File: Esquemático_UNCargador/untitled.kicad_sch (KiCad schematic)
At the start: 17 parts

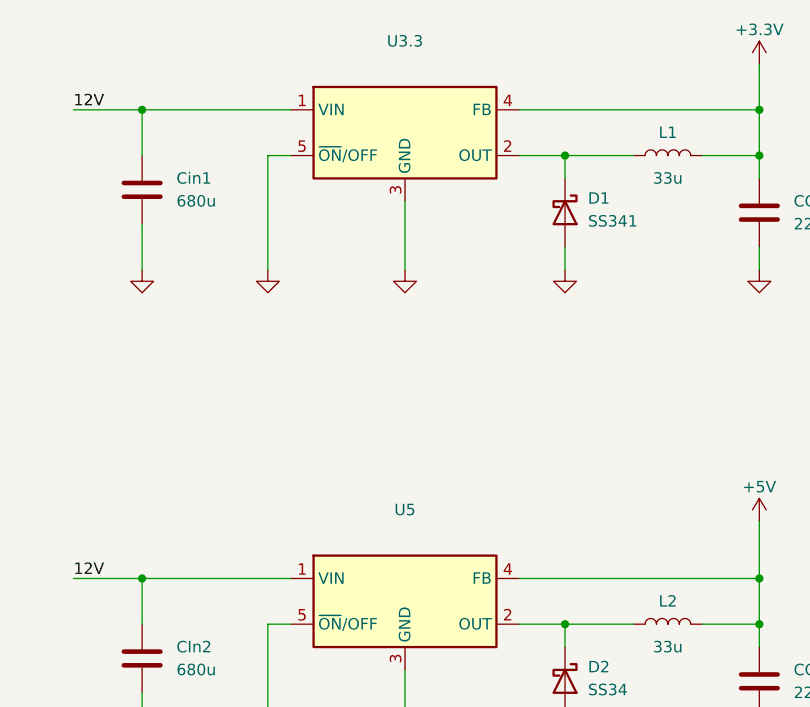
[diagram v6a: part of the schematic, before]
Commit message: LM2596-HuellaActualizada
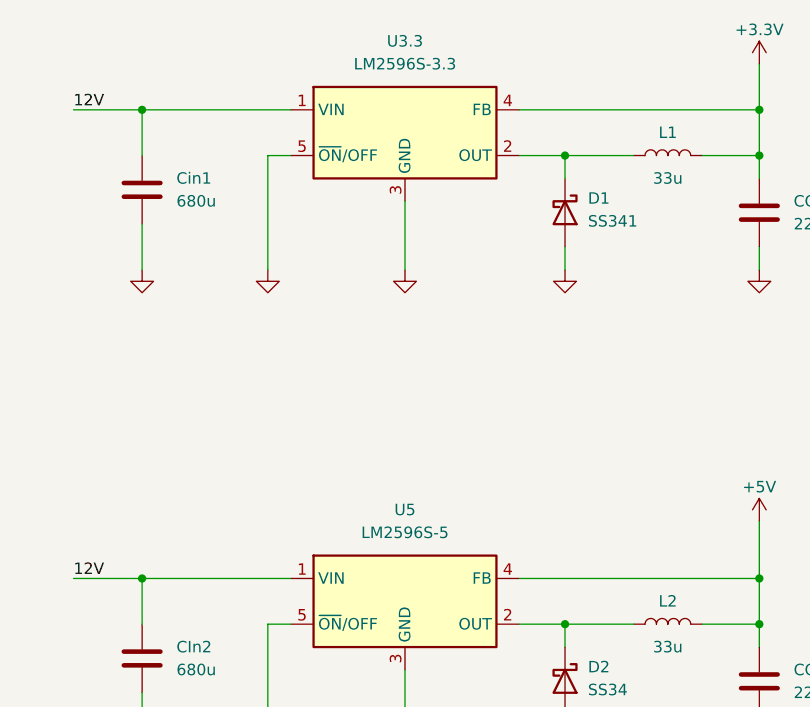
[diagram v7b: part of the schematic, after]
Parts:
- U3.3: value ~ -> LM2596S-3.3; footprint (none) -> Package_TO_SOT_SMD:TO-263-5_TabPin3
- U5: value ~ -> LM2596S-5; footprint (none) -> Package_TO_SOT_SMD:TO-263-5_TabPin3
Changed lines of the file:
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@@
       (effects (font (size 1.27 1.27)))
     )
-    (property "Value" "~" (at 222.25 43.18 0)
-      (effects (font (size 1.27 1.27)))
-    )
-    (property "Footprint" "" (at 223.52 57.15 0)
+    (property "Value" "LM2596S-3.3" (at 222.25 43.18 0)
+      (effects (font (size 1.27 1.27)))
+    )
+    (property "Footprint" "Package_TO_SOT_SMD:TO-263-5_TabPin3" (at 223.52 57.15 0)
       (effects (font (size 1.27 1.27) italic) (justify left) hide)
     )
@@
       (effects (font (size 1.27 1.27)))
     )
-    (property "Value" "~" (at 222.25 95.25 0)
-      (effects (font (size 1.27 1.27)))
-    )
-    (property "Footprint" "" (at 223.52 109.22 0)
+    (property "Value" "LM2596S-5" (at 222.25 95.25 0)
+      (effects (font (size 1.27 1.27)))
+    )
+    (property "Footprint" "Package_TO_SOT_SMD:TO-263-5_TabPin3" (at 223.52 109.22 0)
       (effects (font (size 1.27 1.27) italic) (justify left) hide)
     )
@@
     (pin "1")
     (instances
-      (project "CircuitoPotencia"
-        (path "/f64e4c48-29c2-4644-b6e3-d55b9152fc29/c38372d7-094a-4ec0-82ac-c3a161d378bf"
+      (project "untitled"
+        (path "/9be105a0-504f-4b07-b004-211a0f61b6b4"
+          (reference "#PWR034") (unit 1)
+        )
+      )
+      (project "CircuitoPotencia"
+        (path "/f64e4c48-29c2-4644-b6e3-d55b9152fc29/c38372d7-094a-4ec0-82ac-c3a161d378bf"

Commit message: zener sensores con huellas
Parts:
- U5: footprint Package_TO_SOT_SMD:TO-263-5_TabPin3 -> Package_TO_SOT_THT:TO-220-5_Vertical
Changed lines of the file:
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@@
       (effects (font (size 1.27 1.27)))
     )
-    (property "Footprint" "Package_TO_SOT_SMD:TO-263-5_TabPin3" (at 223.52 109.22 0)
+    (property "Footprint" "Package_TO_SOT_THT:TO-220-5_Vertical" (at 223.52 109.22 0)
       (effects (font (size 1.27 1.27) italic) (justify left) hide)
     )
